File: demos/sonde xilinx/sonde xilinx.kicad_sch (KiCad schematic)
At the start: 25 parts, among them J1 DB25MALE, J2 DB9MALE, P1 CONN_6, U1 74LS125, U2 74LS125

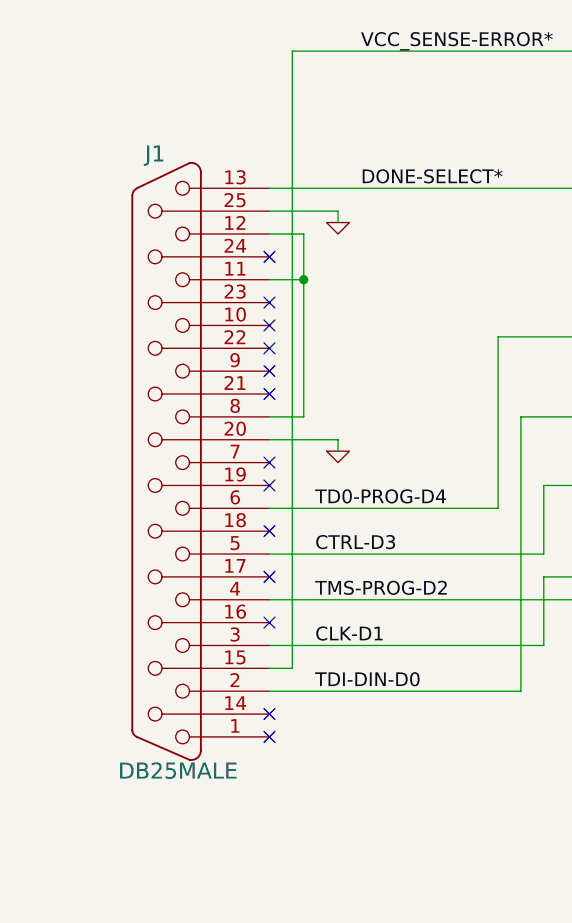
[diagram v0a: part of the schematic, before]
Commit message: feat: update kicad to 9.0.0+dfsg-1
Signed-off-by: lhdjply <lhdjply@126.com>
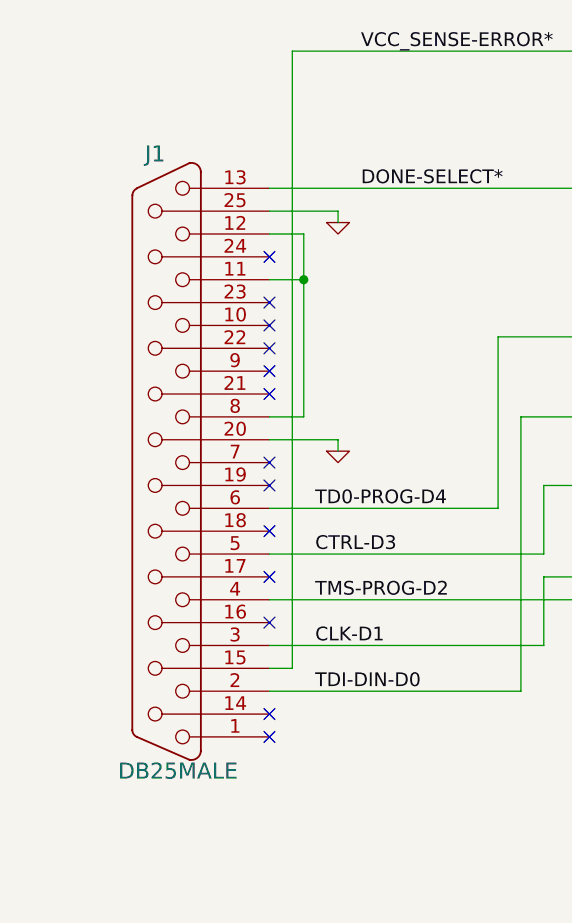
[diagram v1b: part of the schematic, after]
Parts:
- C1: symbol sonde_xilinx_schlib:CP -> sonde_xilinx:CP
- C2, C3, C4, C5: symbol sonde_xilinx_schlib:C -> sonde_xilinx:C
- D1, D2: symbol sonde_xilinx_schlib:DIODESCH -> sonde_xilinx:DIODESCH
- J1: symbol sonde_xilinx_schlib:DB25 -> sonde_xilinx:DB25
- J2: symbol sonde_xilinx_schlib:DB9 -> sonde_xilinx:DB9
- P1: symbol sonde_xilinx_schlib:CONN_6 -> sonde_xilinx:CONN_6
- R1, R10, R11, R12, R13, R14, R2, R4, R5, R6, R7, R8, R9: symbol sonde_xilinx_schlib:R -> sonde_xilinx:R
- U1: symbol sonde_xilinx_schlib:74LS125 -> sonde_xilinx:74LS125_1
- U1: symbol sonde_xilinx_schlib:74LS125 -> sonde_xilinx:74LS125_6
- U1: symbol sonde_xilinx_schlib:74LS125 -> sonde_xilinx:74LS125_7
- U1: symbol sonde_xilinx_schlib:74LS125 -> sonde_xilinx:74LS125
- U2: symbol sonde_xilinx_schlib:74LS125 -> sonde_xilinx:74LS125_2
- U2: symbol sonde_xilinx_schlib:74LS125 -> sonde_xilinx:74LS125_3
- U2: symbol sonde_xilinx_schlib:74LS125 -> sonde_xilinx:74LS125_4
- U2: symbol sonde_xilinx_schlib:74LS125 -> sonde_xilinx:74LS125_5
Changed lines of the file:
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@@
 (kicad_sch
-	(version 20231120)
+	(version 20250114)
 	(generator "eeschema")
-	(generator_version "7.99")
+	(generator_version "9.0")
 	(paper "A4")
 	(title_block
@@
 	(label "TMS-PROG"
 		(at 205.74 96.52 90)
-		(fields_autoplaced yes)
 		(effects
 			(font
@@
 	(label "TDI-DIN-D0"
 		(at 60.96 96.52 0)
-		(fields_autoplaced yes)
 		(effects
 			(font
@@
 	(label "CTRL-D3"
 		(at 60.96 81.28 0)
-		(fields_autoplaced yes)
 		(effects
 			(font
@@
 	(label "PWR_3,3-5V"
 		(at 240.03 88.9 0)
-		(fields_autoplaced yes)
 		(effects
 			(font
@@
 	(label "VCC_SENSE-ERROR*"
 		(at 66.04 25.4 0)
-		(fields_autoplaced yes)
 		(effects
 			(font
@@
 	(label "TD0-PROG-D4"
 		(at 60.96 76.2 0)
-		(fields_autoplaced yes)
 		(effects
 			(font
@@
 	(label "TMS-PROG"
 		(at 191.77 77.47 0)
-		(fields_autoplaced yes)
 		(effects
 			(font
@@
 	(label "TMS-PROG-D2"
 		(at 60.96 86.36 0)
-		(fields_autoplaced yes)
 		(effects
 			(font
@@
 	(label "CLK-D1"
 		(at 60.96 91.44 0)
-		(fields_autoplaced yes)
 		(effects
 			(font
@@
 	(label "DONE-SELECT*"
 		(at 66.04 40.64 0)
-		(fields_autoplaced yes)
 		(effects
 			(font
@@
 	(label "TD0-DONE"
 		(at 191.77 69.85 0)
-		(fields_autoplaced yes)
 		(effects
 			(font
@@
 	(label "TDI-DIN"
 		(at 191.77 72.39 0)
-		(fields_autoplaced yes)
 		(effects
 			(font
@@
 	(label "TCK-CCLK"
 		(at 191.77 74.93 0)
-		(fields_autoplaced yes)
 		(effects
 			(font
@@
 	(label "PWR_3,3-5V"
 		(at 195.58 64.77 0)
-		(fields_autoplaced yes)
 		(effects
 			(font
@@
 	)
 	(symbol
-		(lib_id "sonde_xilinx_schlib:DB25")
+		(lib_id "sonde_xilinx:DB25")
 		(at 44.45 71.12 0)
 		(mirror y)
@@
 	)
 	(symbol
-		(lib_id "sonde_xilinx_schlib:R")
+		(lib_id "sonde_xilinx:R")
 		(at 100.33 25.4 270)
 		(unit 1)
@@
 	)
 	(symbol
-		(lib_id "sonde_xilinx_schlib:R")
+		(lib_id "sonde_xilinx:R")
 		(at 100.33 40.64 270)
 		(unit 1)
@@
 	)
 	(symbol
-		(lib_id "sonde_xilinx_schlib:R")
+		(lib_id "sonde_xilinx:R")
 		(at 100.33 57.15 270)
 		(unit 1)
@@
 	)
 	(symbol
-		(lib_id "sonde_xilinx_schlib:R")
+		(lib_id "sonde_xilinx:R")
 		(at 100.33 83.82 270)
 		(unit 1)
@@
 	)
 	(symbol
-		(lib_id "sonde_xilinx_schlib:R")
+		(lib_id "sonde_xilinx:R")
 		(at 100.33 106.68 270)
 		(unit 1)
@@
 	(symbol
 		(lib_name "74LS125_2")
-		(lib_id "sonde_xilinx_schlib:74LS125")
+		(lib_id "sonde_xilinx:74LS125_2")
 		(at 118.11 40.64 0)
 		(mirror y)
@@
 	(symbol
 		(lib_name "74LS125_1")
-		(lib_id "sonde_xilinx_schlib:74LS125")
+		(lib_id "sonde_xilinx:74LS125_1")
 		(at 137.16 48.26 0)
 		(unit 1)
@@
 	(symbol
 		(lib_name "74LS125_6")
-		(lib_id "sonde_xilinx_schlib:74LS125")
+		(lib_id "sonde_xilinx:74LS125_6")
 		(at 138.43 66.04 0)
 		(unit 2)
@@
 	(symbol
 		(lib_name "74LS125_7")
-		(lib_id "sonde_xilinx_schlib:74LS125")
+		(lib_id "sonde_xilinx:74LS125_7")
 		(at 138.43 83.82 0)
 		(unit 3)
@@
 	)
 	(symbol
-		(lib_id "sonde_xilinx_schlib:74LS125")
+		(lib_id "sonde_xilinx:74LS125")
 		(at 138.43 106.68 0)
 		(unit 4)
@@
 	(symbol
 		(lib_name "74LS125_3")
-		(lib_id "sonde_xilinx_schlib:74LS125")
+		(lib_id "sonde_xilinx:74LS125_3")
 		(at 43.18 175.26 0)
 		(unit 2)
@@
 	(symbol
 		(lib_name "74LS125_4")
-		(lib_id "sonde_xilinx_schlib:74LS125")
+		(lib_id "sonde_xilinx:74LS125_4")
 		(at 43.18 158.75 0)
 		(unit 3)
@@
 	(symbol
 		(lib_name "74LS125_5")
-		(lib_id "sonde_xilinx_schlib:74LS125")
+		(lib_id "sonde_xilinx:74LS125_5")
 		(at 43.18 142.24 0)
 		(unit 4)
@@
 	)
 	(symbol
-		(lib_id "sonde_xilinx_schlib:GND")
+		(lib_id "sonde_xilinx:GND")
 		(at 29.21 185.42 0)
 		(unit 1)
@@
 	)
 	(symbol
-		(lib_id "sonde_xilinx_schlib:GND")
+		(lib_id "sonde_xilinx:GND")
 		(at 118.11 50.8 0)
 		(unit 1)
@@
 	)
 	(symbol
-		(lib_id "sonde_xilinx_schlib:GND")
+		(lib_id "sonde_xilinx:GND")
 		(at 63.5 44.45 0)
 		(unit 1)
@@
 	)
 	(symbol
-		(lib_id "sonde_xilinx_schlib:DIODESCH")
+		(lib_id "sonde_xilinx:DIODESCH")
 		(at 114.3 25.4 0)
 		(mirror y)
@@
 	)
 	(symbol
-		(lib_id "sonde_xilinx_schlib:DIODESCH")
+		(lib_id "sonde_xilinx:DIODESCH")
 		(at 180.34 25.4 0)
 		(mirror y)
@@
 	)
 	(symbol
-		(lib_id "sonde_xilinx_schlib:R")
+		(lib_id "sonde_xilinx:R")
 		(at 149.86 33.02 0)
 		(unit 1)
@@
 	)
 	(symbol
-		(lib_id "sonde_xilinx_schlib:R")
+		(lib_id "sonde_xilinx:R")
 		(at 157.48 33.02 0)
 		(unit 1)
@@
 	)
 	(symbol
-		(lib_id "sonde_xilinx_schlib:R")
+		(lib_id "sonde_xilinx:R")
 		(at 168.91 48.26 270)
 		(unit 1)
@@
 	)
 	(symbol
-		(lib_id "sonde_xilinx_schlib:C")
+		(lib_id "sonde_xilinx:C")
 		(at 160.02 113.03 0)
 		(unit 1)
@@
 	)
 	(symbol
-		(lib_id "sonde_xilinx_schlib:GND")
+		(lib_id "sonde_xilinx:GND")
 		(at 160.02 119.38 0)
 		(unit 1)
@@
 	)
 	(symbol
-		(lib_id "sonde_xilinx_schlib:GND")
+		(lib_id "sonde_xilinx:GND")
 		(at 157.48 40.64 0)
 		(unit 1)
@@
 	)
 	(symbol
-		(lib_id "sonde_xilinx_schlib:CP")
+		(lib_id "sonde_xilinx:CP")
 		(at 165.1 31.75 0)
 		(unit 1)
@@
 	)
 	(symbol
-		(lib_id "sonde_xilinx_schlib:GND")
+		(lib_id "sonde_xilinx:GND")
 		(at 165.1 38.1 0)
 		(unit 1)
@@
 	)
 	(symbol
-		(lib_id "sonde_xilinx_schlib:CONN_6")
+		(lib_id "sonde_xilinx:CONN_6")
 		(at 224.79 71.12 0)
 		(unit 1)
@@
 	)
 	(symbol
-		(lib_id "sonde_xilinx_schlib:GND")
+		(lib_id "sonde_xilinx:GND")
 		(at 214.63 67.31 270)
 		(unit 1)
@@
 	)
 	(symbol
-		(lib_id "sonde_xilinx_schlib:PWR_FLAG")
+		(lib_id "sonde_xilinx:PWR_FLAG")
 		(at 259.08 121.92 0)
 		(unit 1)
@@
 	)
 	(symbol
-		(lib_id "sonde_xilinx_schlib:GND")
+		(lib_id "sonde_xilinx:GND")
 		(at 259.08 123.19 0)
 		(unit 1)
@@
 	)
 	(symbol
-		(lib_id "sonde_xilinx_schlib:VCC")
+		(lib_id "sonde_xilinx:VCC")
 		(at 147.32 24.13 0)
 		(unit 1)
@@
 	)
 	(symbol
-		(lib_id "sonde_xilinx_schlib:PWR_FLAG")
+		(lib_id "sonde_xilinx:PWR_FLAG")
 		(at 154.94 24.13 0)
 		(unit 1)
@@
 	)
 	(symbol
-		(lib_id "sonde_xilinx_schlib:DB9")
+		(lib_id "sonde_xilinx:DB9")
 		(at 271.78 99.06 0)
 		(mirror x)
@@
 	)
 	(symbol
-		(lib_id "sonde_xilinx_schlib:R")
+		(lib_id "sonde_xilinx:R")
 		(at 168.91 66.04 270)
 		(unit 1)
@@
 	)
 	(symbol
-		(lib_id "sonde_xilinx_schlib:R")
+		(lib_id "sonde_xilinx:R")
 		(at 100.33 66.04 270)
 		(unit 1)
@@
 	)
 	(symbol
-		(lib_id "sonde_xilinx_schlib:R")
+		(lib_id "sonde_xilinx:R")
 		(at 100.33 73.66 270)
 		(unit 1)
@@
 	)
 	(symbol
-		(lib_id "sonde_xilinx_schlib:GND")
+		(lib_id "sonde_xilinx:GND")
 		(at 63.5 69.85 0)
 		(unit 1)
@@
 	)
 	(symbol
-		(lib_id "sonde_xilinx_schlib:R")
+		(lib_id "sonde_xilinx:R")
 		(at 168.91 106.68 270)
 		(unit 1)
@@
 	)
 	(symbol
-		(lib_id "sonde_xilinx_schlib:R")
+		(lib_id "sonde_xilinx:R")
 		(at 168.91 83.82 270)
 		(unit 1)
@@
 	)
 	(symbol
-		(lib_id "sonde_xilinx_schlib:C")
+		(lib_id "sonde_xilinx:C")
 		(at 160.02 54.61 0)
 		(unit 1)
@@
 	)
 	(symbol
-		(lib_id "sonde_xilinx_schlib:C")
+		(lib_id "sonde_xilinx:C")
 		(at 160.02 72.39 0)
 		(unit 1)
@@
 	)
 	(symbol
-		(lib_id "sonde_xilinx_schlib:C")
+		(lib_id "sonde_xilinx:C")
 		(at 160.02 90.17 0)
 		(unit 1)
@@
 	)
 	(symbol
-		(lib_id "sonde_xilinx_schlib:GND")
+		(lib_id "sonde_xilinx:GND")
 		(at 160.02 60.96 0)
 		(unit 1)
@@
 	)
 	(symbol
-		(lib_id "sonde_xilinx_schlib:GND")
+		(lib_id "sonde_xilinx:GND")
 		(at 160.02 78.74 0)
 		(unit 1)
@@
 	)
 	(symbol
-		(lib_id "sonde_xilinx_schlib:GND")
+		(lib_id "sonde_xilinx:GND")
 		(at 160.02 96.52 0)
 		(unit 1)
@@
 	)
 	(symbol
-		(lib_id "sonde_xilinx_schlib:GND")
+		(lib_id "sonde_xilinx:GND")
 		(at 255.27 91.44 270)
 		(unit 1)
@@
 	)
 	(symbol
-		(lib_id "sonde_xilinx_schlib:GND")
+		(lib_id "sonde_xilinx:GND")
 		(at 125.73 50.8 0)
 		(unit 1)
@@
 		)
 	)
+	(embedded_fonts no)
 )
